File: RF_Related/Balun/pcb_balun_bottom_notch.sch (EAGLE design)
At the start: 4 parts, among them T1 ADT1-1WT+, X1 SMA-142-0701-801/806, X2 SMA-142-0701-801/806, X3 SMA-142-0701-801/806

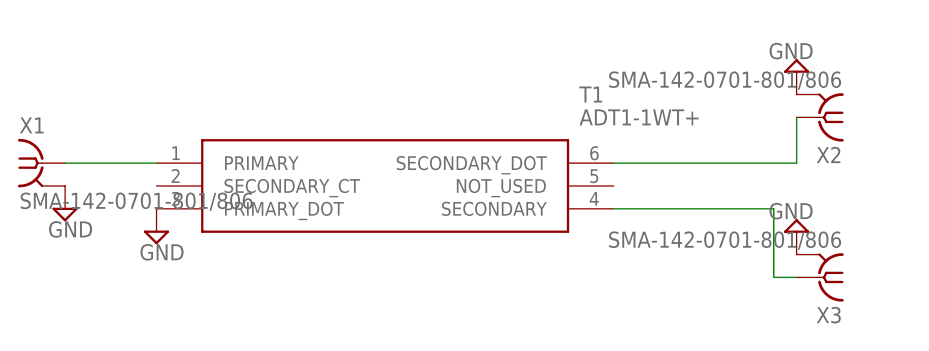
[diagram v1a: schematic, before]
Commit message: doing a second revision of balun boards. going to do another rev of the payload bays soon.
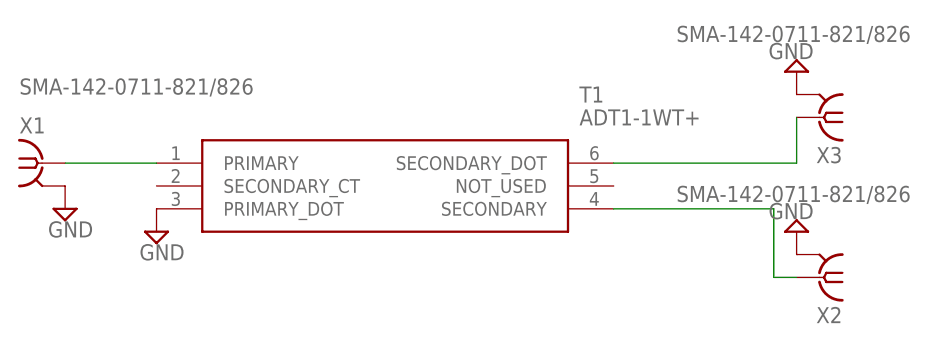
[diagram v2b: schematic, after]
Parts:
- X1: value SMA-142-0701-801/806 -> SMA-142-0711-821/826; device con-coax_flange_mount_edit:SMA-142-0701-801/806 -> con-coax:SMA-142-0711-821/826
- X2, X3: value SMA-142-0701-801/806 -> SMA-142-0711-821/826; device con-coax:SMA-142-0701-801/806 -> con-coax:SMA-142-0711-821/826
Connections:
- net N$2: now also X3.1; no longer X2.1
- net N$3: now also X2.1; no longer X3.1
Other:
- moved on the sheet: X2, X3
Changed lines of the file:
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@@
 <part name="T1" library="ADT1-1WT+" deviceset="ADT1-1WT+" device="" override_package3d_urn="urn:adsk.eagle:package:23639937/2" override_package_urn="urn:adsk.eagle:footprint:23639938/1"/>
 <part name="FRAME1" library="frames" library_urn="urn:adsk.eagle:library:229" deviceset="LETTER_L" device=""/>
-<part name="X1" library="con-coax_flange_mount_edit" deviceset="SMA-" device="142-0701-801/806" package3d_urn="urn:adsk.eagle:package:6214/1" override_package3d_urn="urn:adsk.eagle:package:23639941/7" override_package_urn="urn:adsk.eagle:footprint:6186/1"/>
 <part name="SUPPLY2" library="supply2" library_urn="urn:adsk.eagle:library:372" deviceset="GND" device=""/>
 <part name="SUPPLY7" library="supply2" library_urn="urn:adsk.eagle:library:372" deviceset="GND" device=""/>
 <part name="SUPPLY1" library="supply2" library_urn="urn:adsk.eagle:library:372" deviceset="GND" device=""/>
 <part name="SUPPLY3" library="supply2" library_urn="urn:adsk.eagle:library:372" deviceset="GND" device=""/>
-<part name="X2" library="con-coax" library_urn="urn:adsk.eagle:library:133" deviceset="SMA-" device="142-0701-801/806" package3d_urn="urn:adsk.eagle:package:6214/1" override_package3d_urn="urn:adsk.eagle:package:23770642/3" override_package_urn="urn:adsk.eagle:footprint:6186/1"/>
-<part name="X3" library="con-coax" library_urn="urn:adsk.eagle:library:133" deviceset="SMA-" device="142-0701-801/806" package3d_urn="urn:adsk.eagle:package:6214/1" override_package3d_urn="urn:adsk.eagle:package:23770646/3" override_package_urn="urn:adsk.eagle:footprint:6186/1"/>
+<part name="X1" library="con-coax" library_urn="urn:adsk.eagle:library:133" deviceset="SMA-" device="142-0711-821/826" package3d_urn="urn:adsk.eagle:package:6224/1" override_package3d_urn="urn:adsk.eagle:package:26491994/2" override_package_urn="urn:adsk.eagle:footprint:6190/1"/>
+<part name="X3" library="con-coax" library_urn="urn:adsk.eagle:library:133" deviceset="SMA-" device="142-0711-821/826" package3d_urn="urn:adsk.eagle:package:6224/1" override_package3d_urn="urn:adsk.eagle:package:26491998/2" override_package_urn="urn:adsk.eagle:footprint:6190/1"/>
+<part name="X2" library="con-coax" library_urn="urn:adsk.eagle:library:133" deviceset="SMA-" device="142-0711-821/826" package3d_urn="urn:adsk.eagle:package:6224/1" override_package3d_urn="urn:adsk.eagle:package:26491998/2" override_package_urn="urn:adsk.eagle:footprint:6190/1"/>
 </parts>
 <sheets>
@@
 <attribute name="DRAWING_NAME" x="139.7" y="24.13" size="2.54" layer="94"/>
 </instance>
-<instance part="X1" gate="G1" x="45.72" y="88.9" smashed="yes">
-<attribute name="VALUE" x="43.18" y="83.82" size="1.778" layer="96"/>
-<attribute name="NAME" x="43.18" y="92.202" size="1.778" layer="95"/>
-</instance>
 <instance part="SUPPLY2" gate="GND" x="48.26" y="83.82" smashed="yes">
 <attribute name="VALUE" x="46.355" y="80.645" size="1.778" layer="96"/>
@@
 <attribute name="VALUE" x="131.445" y="84.455" size="1.778" layer="96" rot="R180"/>
 </instance>
-<instance part="X2" gate="G1" x="132.08" y="93.98" smashed="yes" rot="R180">
-<attribute name="VALUE" x="134.62" y="99.06" size="1.778" layer="96" rot="R180"/>
+<instance part="X1" gate="G1" x="45.72" y="88.9" smashed="yes">
+<attribute name="VALUE" x="43.18" y="96.52" size="1.778" layer="96"/>
+<attribute name="NAME" x="43.18" y="92.202" size="1.778" layer="95"/>
+</instance>
+<instance part="X3" gate="G1" x="132.08" y="93.98" smashed="yes" rot="R180">
+<attribute name="VALUE" x="142.24" y="104.14" size="1.778" layer="96" rot="R180"/>
 <attribute name="NAME" x="134.62" y="90.678" size="1.778" layer="95" rot="R180"/>
 </instance>
-<instance part="X3" gate="G1" x="132.08" y="76.2" smashed="yes" rot="R180">
-<attribute name="VALUE" x="134.62" y="81.28" size="1.778" layer="96" rot="R180"/>
+<instance part="X2" gate="G1" x="132.08" y="76.2" smashed="yes" rot="R180">
+<attribute name="VALUE" x="142.24" y="86.36" size="1.778" layer="96" rot="R180"/>
 <attribute name="NAME" x="134.62" y="72.898" size="1.778" layer="95" rot="R180"/>
 </instance>
@@
 <net name="N$1" class="0">
 <segment>
-<pinref part="X1" gate="G1" pin="1"/>
 <pinref part="T1" gate="G$1" pin="PRIMARY"/>
 <wire x1="48.26" y1="88.9" x2="58.42" y2="88.9" width="0.1524" layer="91"/>
+<pinref part="X1" gate="G1" pin="1"/>
 </segment>
 </net>
 <net name="GND" class="0">
-<segment>
-<pinref part="X1" gate="G1" pin="2"/>
-<pinref part="SUPPLY2" gate="GND" pin="GND"/>
-</segment>
 <segment>
 <pinref part="T1" gate="G$1" pin="PRIMARY_DOT"/>
@@
 </segment>
 <segment>
+<pinref part="SUPPLY2" gate="GND" pin="GND"/>
+<pinref part="X1" gate="G1" pin="2"/>
+</segment>
+<segment>
 <pinref part="SUPPLY1" gate="GND" pin="GND"/>
-<pinref part="X2" gate="G1" pin="2"/>
+<pinref part="X3" gate="G1" pin="2"/>
 </segment>
 <segment>
 <pinref part="SUPPLY3" gate="GND" pin="GND"/>
-<pinref part="X3" gate="G1" pin="2"/>
+<pinref part="X2" gate="G1" pin="2"/>
 </segment>
 </net>
@@
 <wire x1="109.22" y1="88.9" x2="129.54" y2="88.9" width="0.1524" layer="91"/>
 <wire x1="129.54" y1="88.9" x2="129.54" y2="93.98" width="0.1524" layer="91"/>
-<pinref part="X2" gate="G1" pin="1"/>
+<pinref part="X3" gate="G1" pin="1"/>
 </segment>
 </net>
@@
 <wire x1="127" y1="83.82" x2="127" y2="76.2" width="0.1524" layer="91"/>
 <wire x1="129.54" y1="76.2" x2="127" y2="76.2" width="0.1524" layer="91"/>
-<pinref part="X3" gate="G1" pin="1"/>
+<pinref part="X2" gate="G1" pin="1"/>
 </segment>
 </net>
